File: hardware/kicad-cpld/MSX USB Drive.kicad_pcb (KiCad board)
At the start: 2 copper layers, 88.9 x 63.6 mm, 9 parts, among them J1 JTAG, J2 CH376, U1 EPM7032_7064, U5 SST39SF040

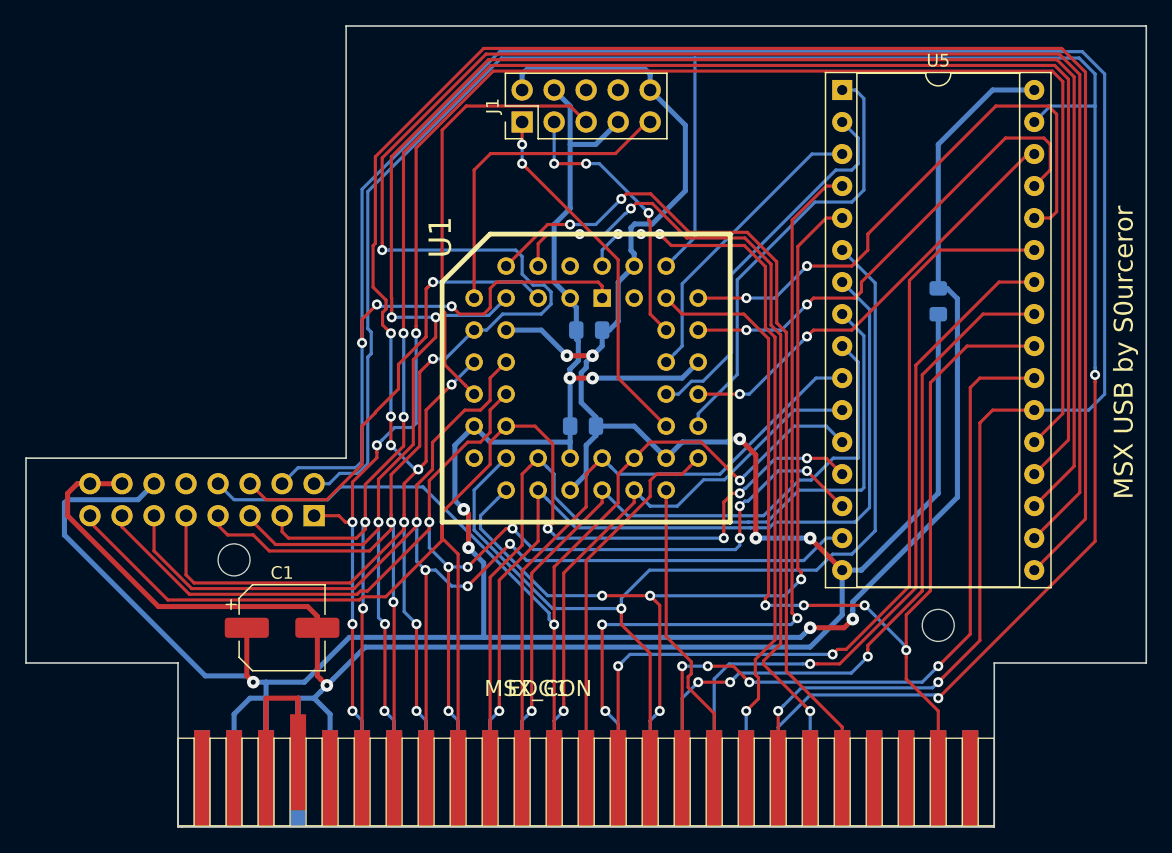
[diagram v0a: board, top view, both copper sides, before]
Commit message: CPLD PCB Verilog + Flash software works
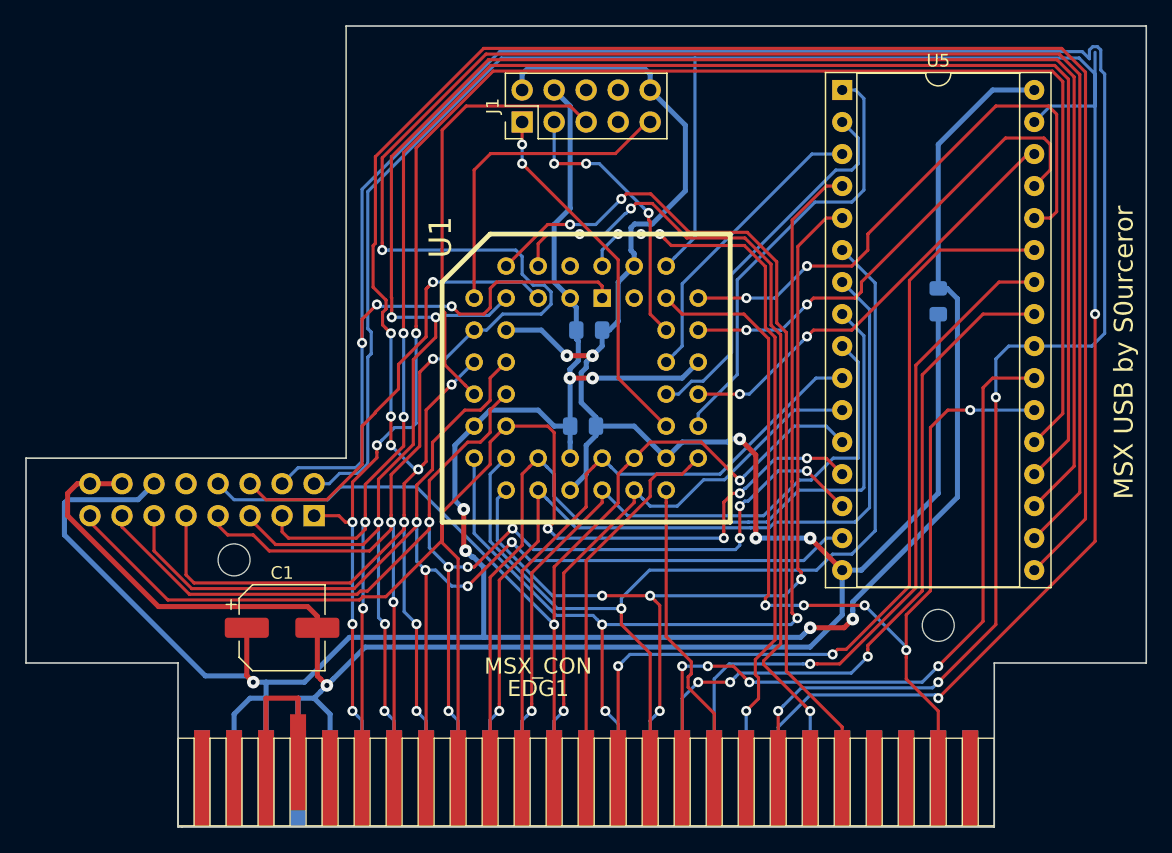
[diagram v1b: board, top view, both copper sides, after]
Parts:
- J1: value JTAG -> AVR-JTAG-10
- J2: value CH376 -> Conn_02x08_Odd_Even
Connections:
- J1 pad 7: VCC -> Net-(J1-Pad7)
- U1 pad 17: Net-(U1-Pad17) -> A12
- U5 pad 22: RD_ -> SLTSL_
- U5 pad 24: SLTSL_ -> RD_
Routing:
- net A12: track 65.3 -> 84.4 mm
- net WR_: track 184.8 -> 189.0 mm
- net VCC: track 224.9 -> 220.7 mm
- net SLTSL_: track 86.2 -> 82.0 mm, vias 4 -> 5
- net RD_: track 194.8 -> 196.3 mm, vias 5 -> 6
- net A7: track 78.2 -> 76.8 mm
- net A6: track 82.0 -> 80.7 mm
- net D0: track 104.6 -> 105.3 mm
- net A10: track 58.8 -> 58.2 mm

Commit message: Discrete PCB discontinued, flash changed AM29F040
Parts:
- U5: value SST39SF040 -> AM29f040
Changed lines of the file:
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@@
       (effects (font (size 1 1) (thickness 0.15)))
     )
-    (fp_text value SST39SF040 (at 7.62 40.43) (layer F.Fab)
+    (fp_text value AM29f040 (at 7.62 40.43) (layer F.Fab)
       (effects (font (size 1 1) (thickness 0.15)))
     )

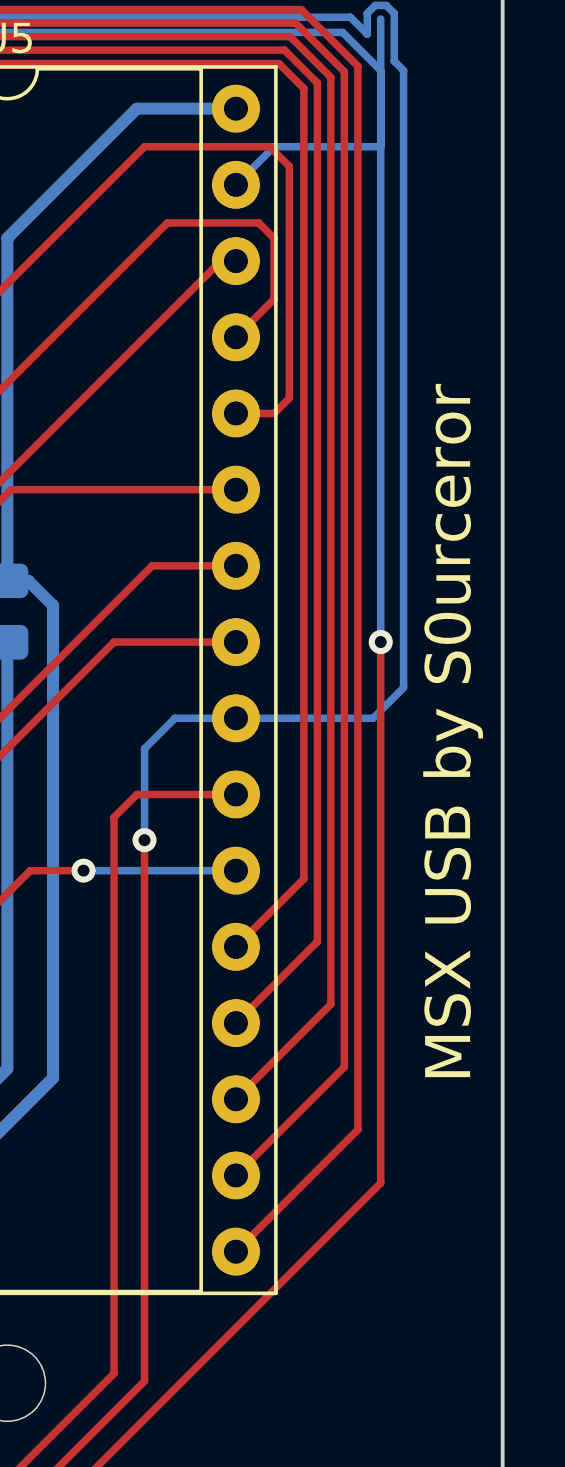
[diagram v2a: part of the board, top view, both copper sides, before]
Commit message: flash support AMIC, new v1.0 Gerbers
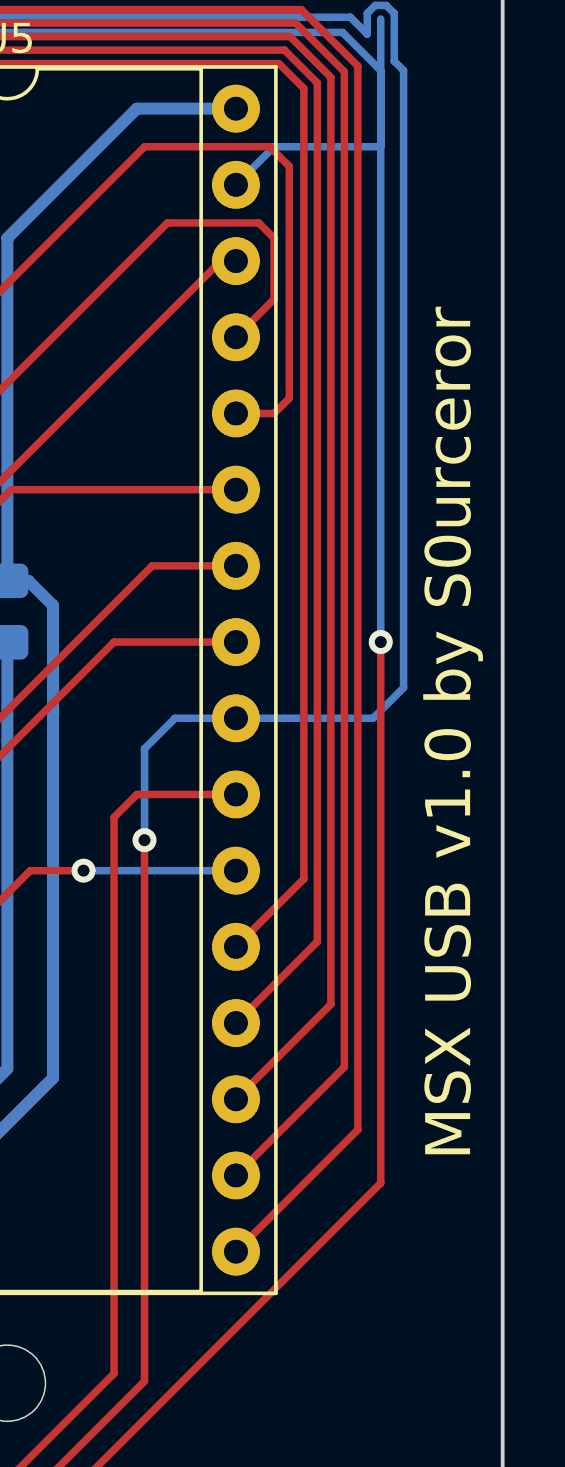
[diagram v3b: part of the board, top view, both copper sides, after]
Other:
- board text added: "MSX USB v1.0 by S0urceror"
- board text removed: "MSX USB by S0urceror"
